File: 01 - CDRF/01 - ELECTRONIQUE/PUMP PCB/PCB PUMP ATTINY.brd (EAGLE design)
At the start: 25.4 x 25.1 mm, 15 parts, among them IC1 ATTINY402-SSN, J3 PWRPAD2-5MM, J4 PWRPAD2-5MM

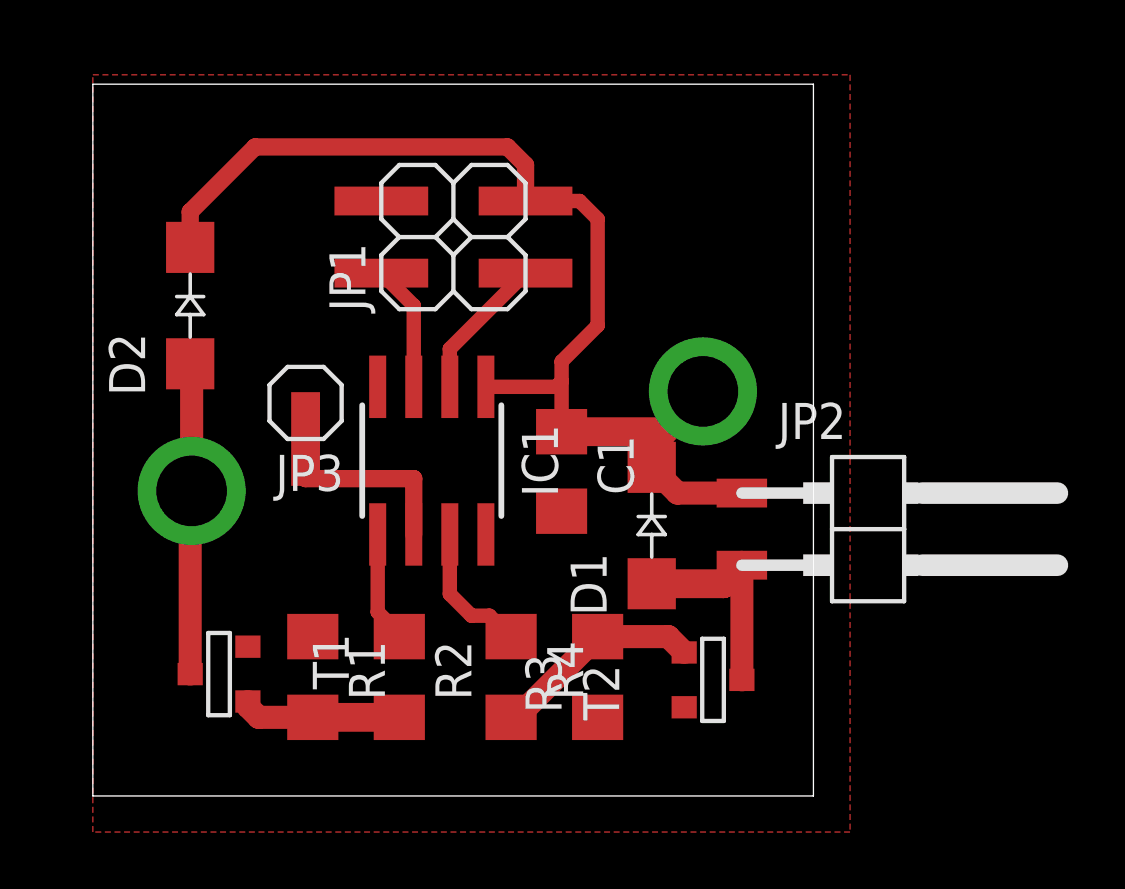
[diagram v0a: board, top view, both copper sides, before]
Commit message: add cap and led
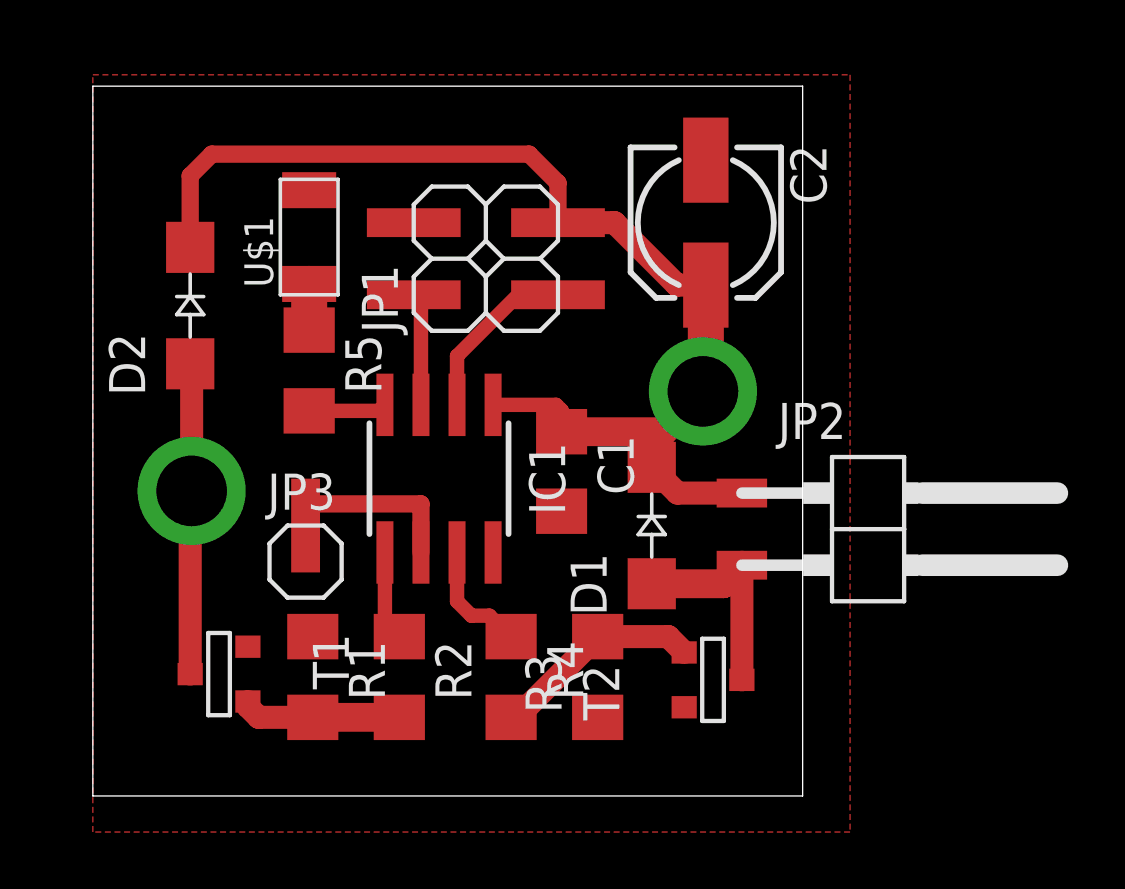
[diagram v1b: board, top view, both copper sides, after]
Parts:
- added C2: (no value), rcl:153CLV-0505
- added R5: 1K, rcl:R1206
- added U$1: LEDFAB1206, fab:LED1206FAB
- moved JP3 6.14 mm to (8.76, 8.26), turned to 0 degrees
- moved JP1 1.37 mm to (12.6, 18.9)
- moved IC1 0.68 mm to (12.2, 11.2)
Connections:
- new net N$6: R5.1, U$1.1
- new net N$7: IC1.4, R5.2
- net +5V: now also C2.+
- net GND: now also C2.-, U$1.2
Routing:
- net N$7: track 0.00 -> 2.75 mm
- net +5V: track 41.8 -> 43.4 mm
- net N$6: track 0.00 -> 1.63 mm
- net TX: track 5.11 -> 6.17 mm
- net PUMP: track 3.91 -> 3.17 mm
- net EV: track 4.88 -> 4.14 mm
- net N$5: track 7.17 -> 6.54 mm
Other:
- board size 25.4 x 25.1 mm -> 25 x 25 mm

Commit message: Fisrt version laser
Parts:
- moved T2 1.14 mm to (20.7, 4.06), turned to 180 degrees
- moved R3 1.02 mm to (16.8, 4.19), turned to 270 degrees
- moved R4 0.89 mm to (13.8, 4.19)
- moved D1 0.25 mm to (19.7, 9.27)
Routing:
- net TX: track 6.17 -> 8.83 mm
- net +5V: track 43.4 -> 45.2 mm
- net N$4: track 7.51 -> 5.98 mm
- net N$1: track 7.48 -> 6.21 mm
- net EV: track 4.14 -> 3.38 mm
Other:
- board size 25 x 25 mm -> 26.3 x 26.3 mm
